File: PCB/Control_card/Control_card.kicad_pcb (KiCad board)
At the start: 2 copper layers, 68.6 x 44.3 mm, 46 parts, among them IC1 TLSR8253F512ET48, J1 Conn_02x04_Counter_Clockwise, J2 Conn_01x01_Pin, J3 Conn_01x01_Pin, J4 Conn_01x01_Pin, J5 Conn_01x01_Pin, Y1 Crystal_GND24

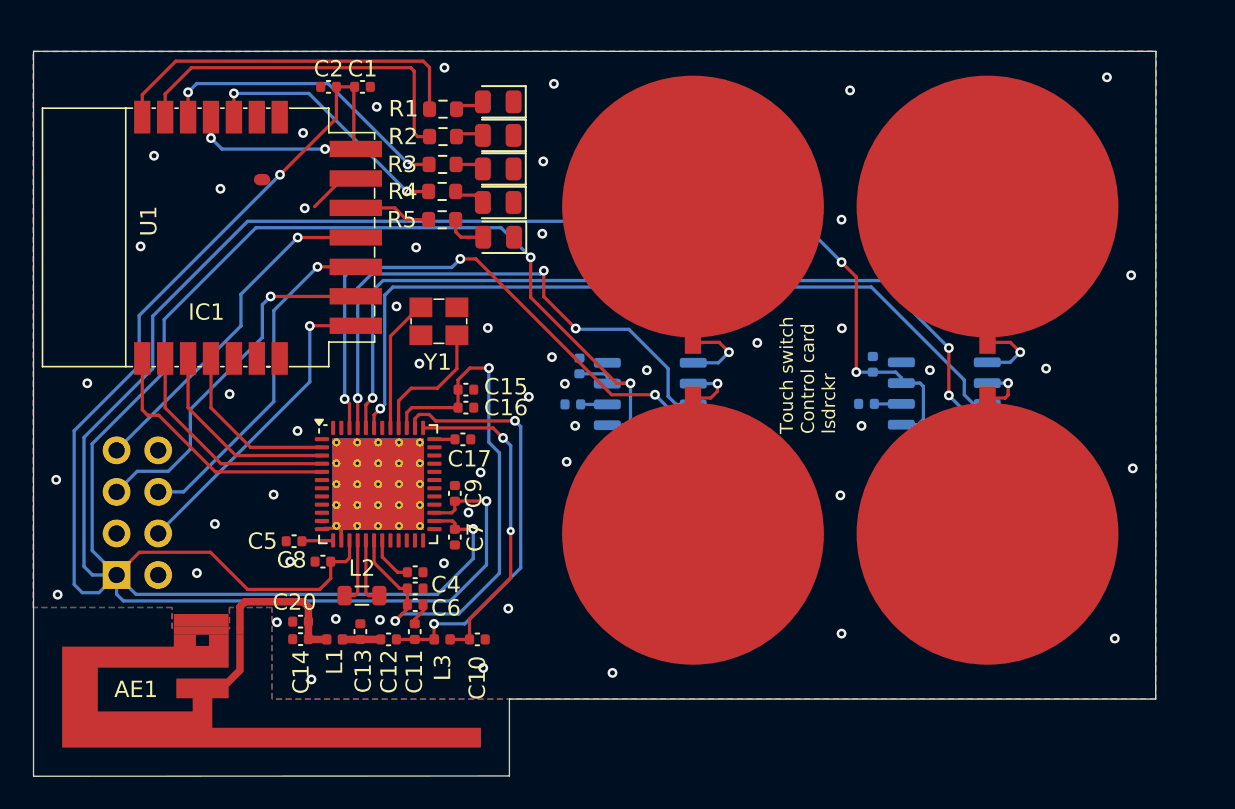
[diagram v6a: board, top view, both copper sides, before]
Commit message: Changement de connecteurs
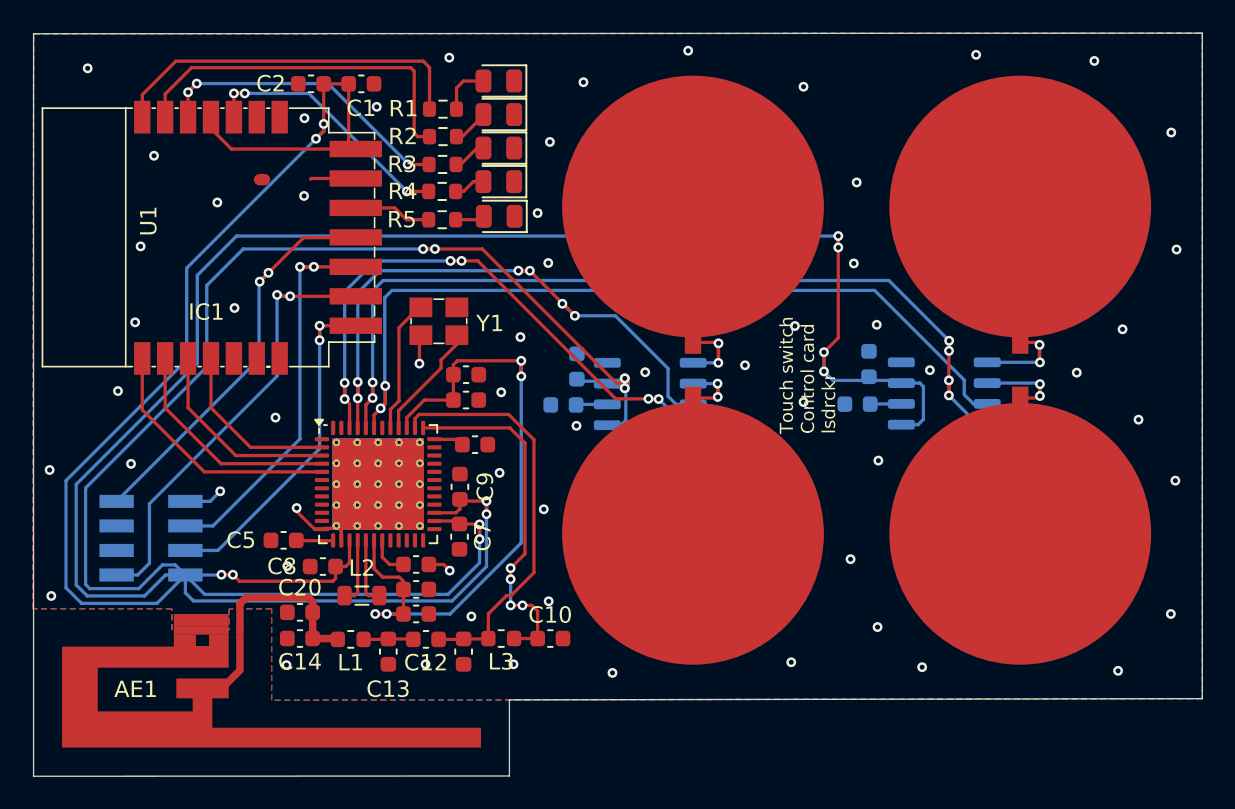
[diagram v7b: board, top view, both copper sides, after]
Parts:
- C1, C10, C11, C12, C13, C14, C15, C16, C17, C2, C20, C21, C22, C23, C24, C3, C4, C5, C6, C7, C8, C9: footprint Capacitor_SMD:C_0402_1005Metric -> Capacitor_SMD:C_0603_1608Metric
- J1: footprint Connector_PinHeader_2.54mm:PinHeader_2x04_P2.54mm_Vertical -> Touch_Switch_Custom:Pin mâle
- L1, L3: footprint Inductor_SMD:L_0402_1005Metric -> Inductor_SMD:L_0603_1608Metric
- moved C10 4.46 mm to (157.1, 83.0)
- moved L3 3.61 mm to (154.1, 83.0)
- moved C11 3.22 mm to (151.8, 83.8), turned to -90 degrees
- moved C12 2.28 mm to (149.5, 83.1)
- moved C13 2.10 mm to (147.2, 83.8), turned to -90 degrees
- moved J2 2.00 mm to (185.8, 56.6)
- moved J3 2.00 mm to (185.8, 76.6)
- moved D1 1.28 mm to (153.9, 48.9)
- moved D3 1.28 mm to (153.9, 53.0)
- moved D2 1.28 mm to (153.9, 51.0)
- moved D4 1.28 mm to (153.9, 55.1)
- moved D5 1.28 mm to (154.0, 57.2)
- moved C2 1.09 mm to (142.5, 49.1)
- moved L1 0.98 mm to (144.9, 83.1)
- moved C15 0.92 mm to (151.9, 66.9)
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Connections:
- J1 pad 1: 3.3V -> CT2
- J1 pad 2: GND -> unconnected-(J1-Pin_2-Pad2)
- J1 pad 4: CT1 -> CT4
- J1 pad 5: CT2 -> GND
- J1 pad 7: CT4 -> CT1
- J1 pad 8: unconnected-(J1-Pin_8-Pad8) -> 3.3V
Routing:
- net 3.3V: track 276.3 -> 288.4 mm, vias 9 -> 16
- net VVD1V2: track 34.8 -> 41.6 mm, vias 2 -> 4
- net GND: track 68.5 -> 74.8 mm, vias 52 -> 60
- net OutSw2: track 51.7 -> 57.2 mm, vias 3 -> 6
- net CT2: track 22.5 -> 27.7 mm, vias 1 -> 2
- net CT4: track 21.0 -> 24.8 mm, vias 1 -> 2
- net CT3: track 21.4 -> 24.8 mm, vias 1 -> 2
- net OutSw3: track 34.8 -> 38.2 mm, vias 3 -> 6
- net Net-(IC1-VANT): track 19.9 -> 23.2 mm, vias 2 -> 4
- net CT1: track 19.2 -> 22.3 mm, vias 1 -> 2
- net Net-(J3-Pin_1): track 3.34 -> 6.15 mm, vias 1 -> 2
- net OutSw4: track 35.3 -> 38.0 mm, vias 3 -> 6
- net Net-(J2-Pin_1): track 4.52 -> 6.63 mm, vias 1 -> 2
- net Net-(J5-Pin_1): track 3.62 -> 5.56 mm, vias 1 -> 2
- net Net-(J4-Pin_1): track 4.90 -> 6.78 mm, vias 1 -> 2
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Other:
- board size 68.6 x 44.3 mm -> 71.4 x 45.4 mm

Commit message: Ajout des footprints
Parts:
- J1: footprint Touch_Switch_Custom:Pin mâle -> Touch_Switch_Custom:PinMale
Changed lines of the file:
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@@
 		)
 	)
-	(footprint "Touch_Switch_Custom:Pin mâle"
+	(footprint "Touch_Switch_Custom:PinMale"
 		(layer "B.Cu")
 		(at 130.593406 79.117611)
 		(property "Reference" "J1"
-			(at 0 11.4 180)
+			(at -2.293406 -3.667611 0)
 			(unlocked yes)
 			(layer "B.SilkS")
@@
 			)
 		)
-		(property "Footprint" "Touch_Switch_Custom:Pin mâle"
+		(property "Footprint" "Touch_Switch_Custom:PinMale"
 			(at 0 10.9 180)
 			(unlocked yes)
